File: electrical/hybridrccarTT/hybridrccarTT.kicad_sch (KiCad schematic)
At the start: 3 parts, among them SW1 RotaryEncoder, U1 STM32F103C8Tx, U2 AMS1117-3.3

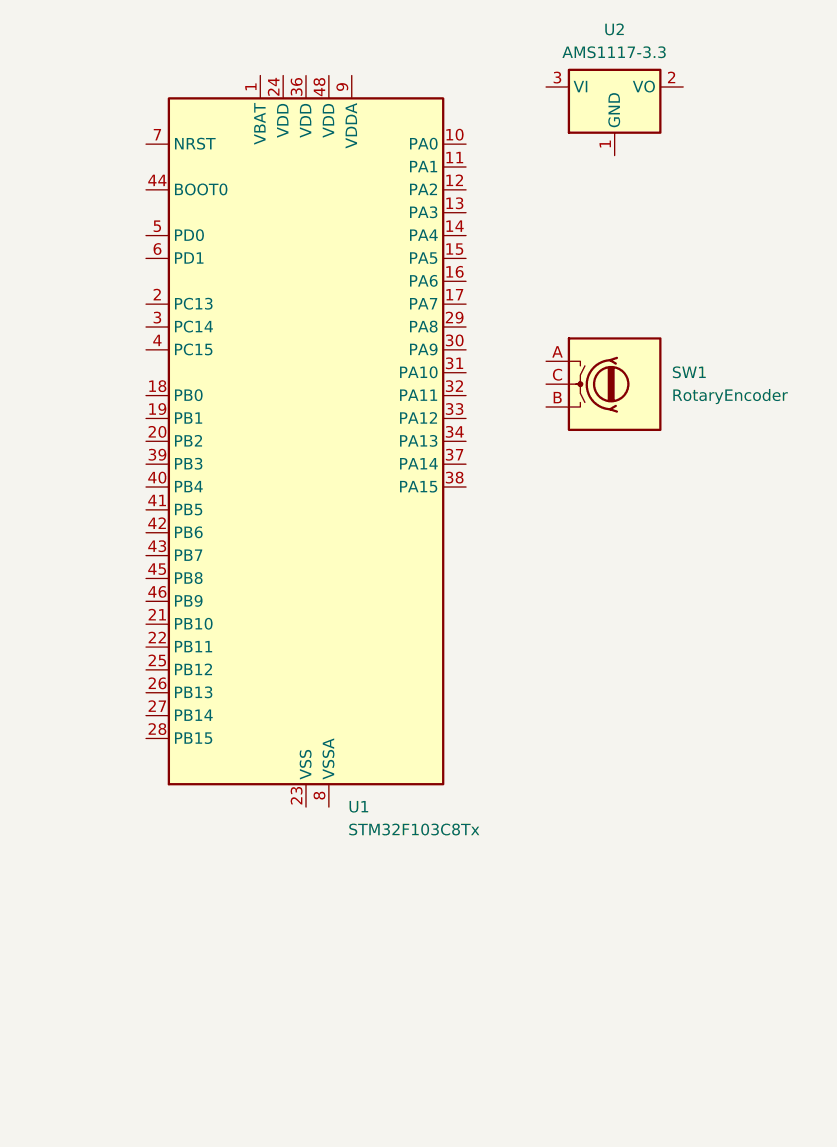
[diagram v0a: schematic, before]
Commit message: edited bluepill color, started sch
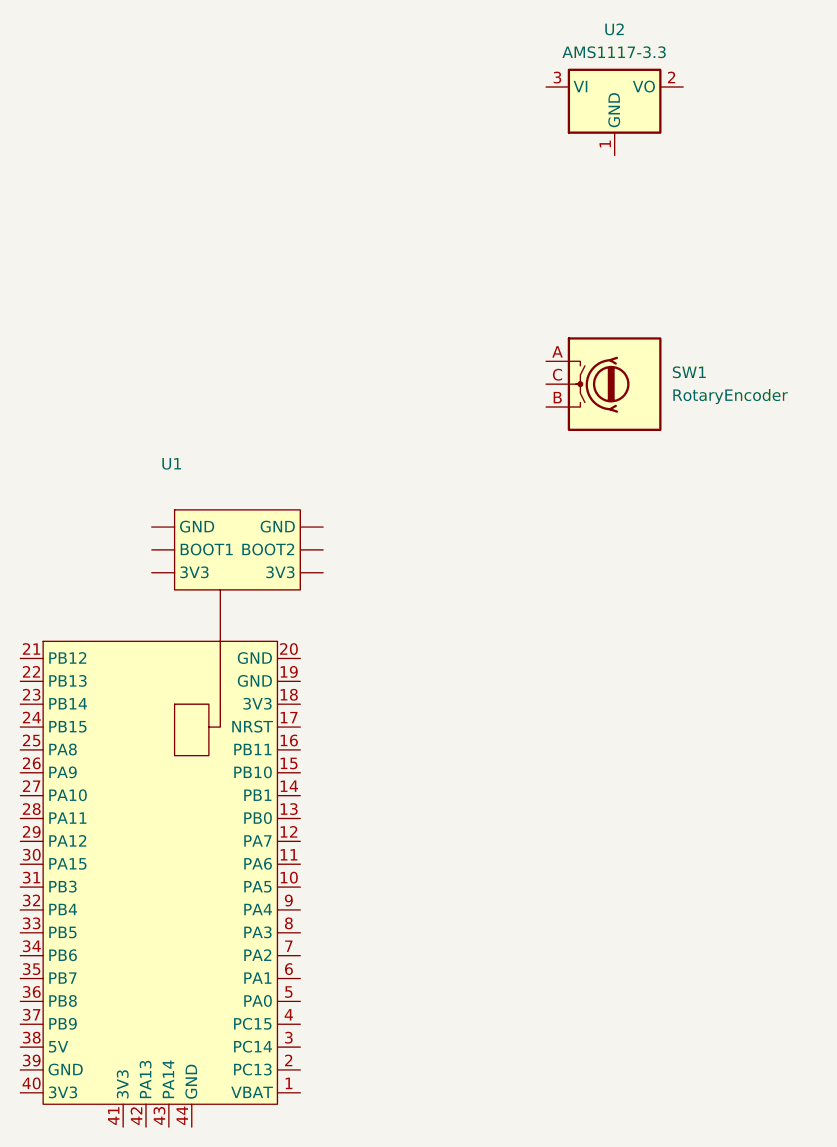
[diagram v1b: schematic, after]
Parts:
- removed U1: STM32F103C8Tx, Package_QFP:LQFP-48_7x7mm_P0.5mm, symbol MCU_ST_STM32F1:STM32F103C8Tx
- added U1: ~, symbol hybridrccarTT-library:bluepill
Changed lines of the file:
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@@
 	)
 	(symbol
-		(lib_id "MCU_ST_STM32F1:STM32F103C8Tx")
-		(at 76.2 97.79 0)
+		(lib_id "hybridrccarTT-library:bluepill")
+		(at 59.69 146.05 0)
 		(unit 1)
 		(exclude_from_sim no)
@@
 		(fields_autoplaced yes)
 		(property "Reference" "U1"
-			(at 80.8833 138.43 0)
+			(at 61.2775 100.33 0)
 			(effects
 				(font
 					(size 1.27 1.27)
 				)
-				(justify left)
 			)
 		)
-		(property "Value" "STM32F103C8Tx"
-			(at 80.8833 140.97 0)
+		(property "Value" "~"
+			(at 61.2775 102.87 0)
 			(effects
 				(font
 					(size 1.27 1.27)
 				)
-				(justify left)
 			)
 		)
-		(property "Footprint" "Package_QFP:LQFP-48_7x7mm_P0.5mm"
-			(at 60.96 135.89 0)
-			(effects
-				(font
-					(size 1.27 1.27)
-				)
-				(justify right)
-				(hide yes)
-			)
-		)
-		(property "Datasheet" "https://www.st.com/resource/en/datasheet/stm32f103c8.pdf"
-			(at 76.2 97.79 0)
+		(property "Footprint" ""
+			(at 59.69 146.05 0)
 			(effects
 				(font
@@
 			)
 		)
-		(property "Description" "STMicroelectronics Arm Cortex-M3 MCU, 64KB flash, 20KB RAM, 72 MHz, 2.0-3.6V, 37 GPIO, LQFP48"
-			(at 76.2 97.79 0)
+		(property "Datasheet" ""
+			(at 59.69 146.05 0)
 			(effects
 				(font
@@
 			)
 		)
-		(pin "16"
+		(property "Description" ""
+			(at 59.69 146.05 0)
+			(effects
+				(font
+					(size 1.27 1.27)
+				)
+				(hide yes)
+			)
 		)
-		(pin "15"
+		(pin "32"
 		)
-		(pin "14"
+		(pin "41"
+		)
+		(pin "30"
+		)
+		(pin ""
+		)
+		(pin "28"
+		)
+		(pin "22"
+		)
+		(pin "34"
+		)
+		(pin "38"
+		)
+		(pin "39"
+		)
+		(pin ""
+		)
+		(pin "21"
+		)
+		(pin "37"
+		)
+		(pin "24"
+		)
+		(pin "26"
 		)
 		(pin "13"
 		)
-		(pin "12"
-		)
-		(pin "11"
-		)
 		(pin "10"
 		)
-		(pin "34"
+		(pin "8"
 		)
 		(pin "33"
 		)
-		(pin "32"
-		)
-		(pin "31"
-		)
-		(pin "30"
-		)
-		(pin "9"
-		)
-		(pin "47"
-		)
-		(pin "48"
-		)
-		(pin "8"
-		)
-		(pin "29"
-		)
-		(pin "17"
-		)
-		(pin "37"
-		)
-		(pin "38"
-		)
-		(pin "43"
-		)
-		(pin "45"
-		)
-		(pin "46"
-		)
-		(pin "3"
-		)
-		(pin "4"
-		)
-		(pin "18"
-		)
-		(pin "19"
-		)
-		(pin "20"
-		)
-		(pin "39"
-		)
-		(pin "40"
-		)
-		(pin "41"
-		)
-		(pin "1"
-		)
-		(pin "28"
+		(pin "25"
 		)
 		(pin "27"
 		)
-		(pin "26"
-		)
-		(pin "25"
-		)
-		(pin "22"
-		)
-		(pin "21"
-		)
-		(pin "7"
-		)
-		(pin "44"
-		)
-		(pin "5"
-		)
-		(pin "6"
-		)
-		(pin "2"
-		)
-		(pin "42"
-		)
-		(pin "24"
-		)
-		(pin "36"
+		(pin "31"
 		)
 		(pin "23"
@@
 		(pin "35"
 		)
+		(pin "29"
+		)
+		(pin "36"
+		)
+		(pin "40"
+		)
+		(pin "42"
+		)
+		(pin ""
+		)
+		(pin "20"
+		)
+		(pin "19"
+		)
+		(pin "43"
+		)
+		(pin "17"
+		)
+		(pin "16"
+		)
+		(pin "14"
+		)
+		(pin "18"
+		)
+		(pin "44"
+		)
+		(pin "12"
+		)
+		(pin "15"
+		)
+		(pin "11"
+		)
+		(pin "9"
+		)
+		(pin "3"
+		)
+		(pin ""
+		)
+		(pin ""
+		)
+		(pin "7"
+		)
+		(pin "1"
+		)
+		(pin "6"
+		)
+		(pin "4"
+		)
+		(pin "2"
+		)
+		(pin "5"
+		)
+		(pin ""
+		)
 		(instances
